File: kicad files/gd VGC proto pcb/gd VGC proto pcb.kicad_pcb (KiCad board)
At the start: 2 copper layers, 104 parts, among them J1 PWR_IN, J10 VID_OUT, J11 RCA MONO OUT, J12 Main Data Bus, J13 Mono-Color, J14 Mono-Color, J15 VBL, J16 RTC, J17 RCA Shunt Select, J18 RCA, J19 CREF, J2 Video Binary B, J20 RGB In, J21 CLKS, J22 Memory Control, J23 VGC Extra, J3 Aux Data Bus, J4 DAC RGB, J5 Video Binary G, J6 COMP_RGB, J7 Video Binary R, J8 RAM Addr Bus, J9 Composite Sync, Q1 BC817, Q2 BC817, Q3 BC817, U1 MIC5504-3.3YM5, U2 28.636360 MHz

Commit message: most of VGC routed
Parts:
- removed TP160, TP189, TP5: TestPoint, My Libraries:Harwin-S1751-46-Test-Point
- added C16: 1000u, Capacitor_THT:CP_Radial_D5.0mm_P2.50mm, F.Cu at (106.7, 75.2)
- added J24: CLK_PH0, Connector_PinHeader_2.54mm:PinHeader_1x02_P2.54mm_Vertical, F.Cu at (129.5, 130.8)
- added J25: Bald-Ext-1, Connector_PinHeader_2.54mm:PinHeader_2x20_P2.54mm_Vertical, F.Cu at (86.4, 80.0)
- added J26: SYNC, Connector_PinHeader_2.54mm:PinHeader_1x02_P2.54mm_Vertical, F.Cu at (121.9, 130.8)
- C59, R11, R196, TP112, TP93: moved to B.Cu
- C61: footprint Capacitor_SMD:C_0805_2012Metric -> Capacitor_THT:CP_Radial_D5.0mm_P2.50mm
- J13: value Mono-Color -> COMSYNC
- J19: footprint Connector_PinHeader_2.54mm:PinHeader_1x02_P2.54mm_Vertical -> Connector_PinHeader_2.54mm:PinHeader_2x02_P2.54mm_Vertical
- J20: footprint Connector_PinHeader_2.54mm:PinHeader_1x04_P2.54mm_Vertical -> Connector_PinHeader_2.54mm:PinHeader_1x08_P2.54mm_Vertical
- J21: value CLKS -> CLK_14M; footprint Connector_PinHeader_2.54mm:PinHeader_1x04_P2.54mm_Vertical -> Connector_PinHeader_2.54mm:PinHeader_1x02_P2.54mm_Vertical
- J22: footprint Connector_PinHeader_2.54mm:PinHeader_1x06_P2.54mm_Vertical -> Connector_PinHeader_2.54mm:PinHeader_2x06_P2.54mm_Vertical
- J23: footprint Connector_PinHeader_2.54mm:PinHeader_1x03_P2.54mm_Vertical -> Connector_PinHeader_2.54mm:PinHeader_2x03_P2.54mm_Vertical
- moved R206 145.1 mm to (100.3, 76.2), turned to 270 degrees
- moved J5 114.3 mm to (120.7, 72.4)
- moved J7 109.5 mm to (130.8, 80.0), turned to 180 degrees
- moved C61 107.1 mm to (130.8, 86.9), turned to 90 degrees
- moved J2 104.4 mm to (141.0, 80.0), turned to 180 degrees
- moved C30 99.4 mm to (127.3, 125.2)
- moved C59 83.3 mm to (137.2, 110.2), turned to 90 degrees
- moved J15 79.0 mm to (143.5, 102.9)
- moved TP112 67.8 mm to (137.2, 114.3), turned to 180 degrees
- moved R30 65.3 mm to (127.3, 127.5), turned to 180 degrees
- moved R196 60.1 mm to (123.7, 126.0), turned to 270 degrees
- moved TP93 57.8 mm to (127.5, 125.7), turned to 90 degrees
- moved R11 52.9 mm to (131.1, 126.0), turned to 270 degrees
- moved J20 29.2 mm to (96.5, 88.9), turned to 0 degrees
- moved J8 20.5 mm to (96.5, 110.5), turned to 0 degrees
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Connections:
- J19 pad 2: CREF.L -> CREF.H
- J20 pad 1: /RGB1.H -> /RGB4.H
- J20 pad 2: /RGB2.H -> /RGB4.H
- J20 pad 3: /RGB4.H -> /RGB8.H
- J21 pad 1: /14M.H -> /14MD.H
- J22 pad 1: /A2R-W.H -> /FLIP6.H
- J22 pad 2: /STRETCH.L -> /FLIP6.H
- J22 pad 4: /FLIP6.H -> /FLIP7.H
- J22 pad 5: /IRQ.L -> /HDSEL.H
- J22 pad 6: /M2SEL.L -> /HDSEL.H
- J23 pad 1: /RESET.L -> /IRQ.L
- J23 pad 2: /HDSEL.H -> /IRQ.L
- J23 pad 3: /BABUS12 -> /RESET.L
- UF2 pad 55: /UG3-6 -> /UG3-1
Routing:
- net /PH0.H: track 0.00 -> 61.5 mm
- net /RABUS6: track 0.00 -> 47.2 mm
- net /RABUS7: track 0.00 -> 46.6 mm
- net /RABUS4: track 0.00 -> 42.7 mm
- net /RABUS2: track 0.00 -> 42.6 mm
- net /RABUS5: track 0.00 -> 41.6 mm
- net /RABUS1: track 0.00 -> 41.0 mm
- net /RABUS3: track 0.00 -> 39.9 mm
- net /RABUS0: track 0.00 -> 38.5 mm
- net /MDBUS6: track 0.00 -> 34.5 mm
- net /MDBUS7: track 0.00 -> 34.1 mm
- net /ADBUS7: track 0.00 -> 30.6 mm
- net /MDBUS4: track 0.00 -> 30.3 mm
- net /ADBUS0: track 0.00 -> 30.1 mm
- net /MDBUS1: track 0.00 -> 30.1 mm
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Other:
- copper layers 2 -> 4
- net class Default: trace_width 0.2032 -> 0.254

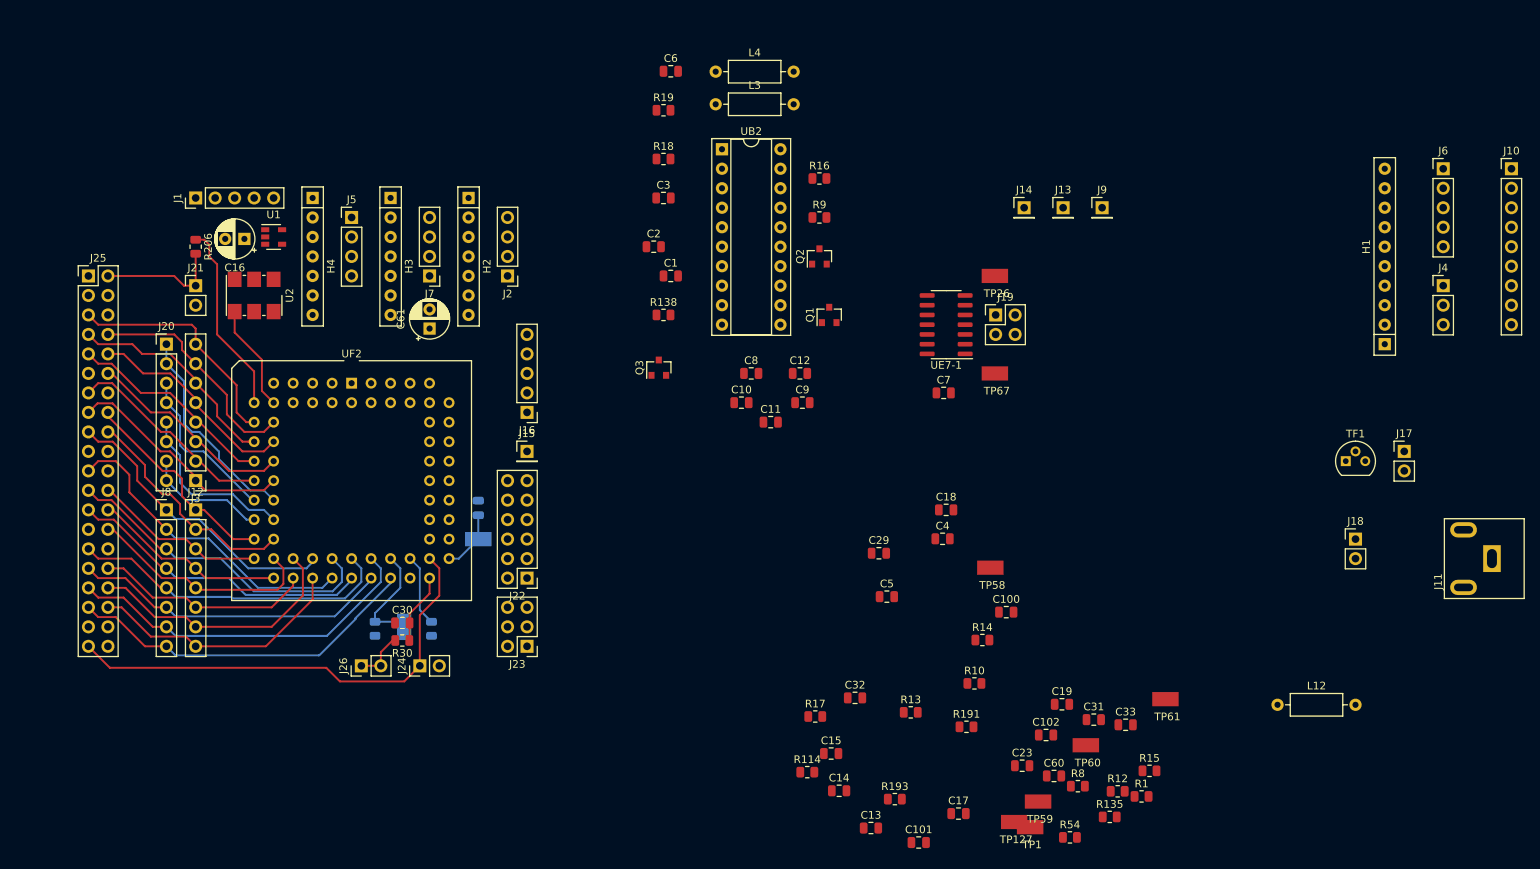
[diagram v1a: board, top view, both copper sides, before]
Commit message: More grouping components by function. Fixed an error with filtering caps on RGB near video output connector.
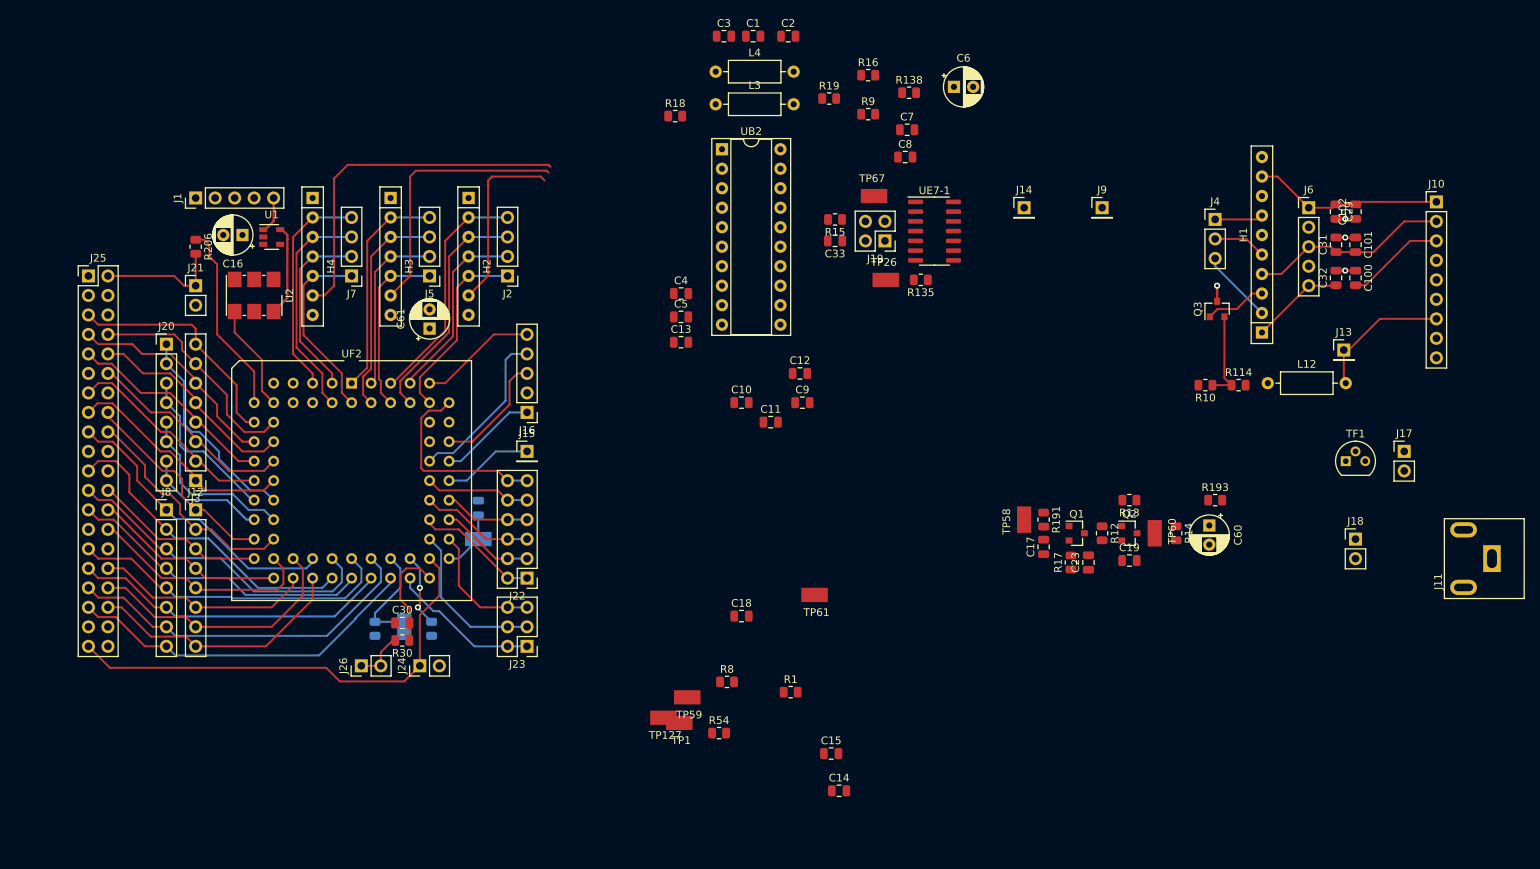
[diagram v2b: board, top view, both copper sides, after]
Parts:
- C6, C60: footprint Capacitor_SMD:C_0805_2012Metric -> Capacitor_THT:CP_Radial_D5.0mm_P2.50mm
- moved C101 96.5 mm to (251.5, 75.9), turned to 270 degrees
- moved C32 83.2 mm to (248.9, 80.3), turned to 90 degrees
- moved R15 82.7 mm to (183.6, 72.6), turned to 180 degrees
- moved C102 79.2 mm to (251.5, 71.6), turned to 90 degrees
- moved R114 75.5 mm to (236.2, 94.2)
- moved C29 74.4 mm to (248.9, 71.6), turned to 270 degrees
- moved R135 74.2 mm to (194.8, 80.5), turned to 180 degrees
- moved C33 73.5 mm to (183.6, 75.4), turned to 180 degrees
- moved Q3 73.1 mm to (233.4, 84.3)
- moved C31 69.5 mm to (248.9, 75.9), turned to 90 degrees
- moved C13 68.0 mm to (163.6, 88.6)
- moved C100 63.0 mm to (251.5, 80.3), turned to 270 degrees
- moved R193 57.1 mm to (233.2, 109.2)
- moved Q2 54.1 mm to (222.0, 113.5), turned to 0 degrees
- moved R10 49.2 mm to (231.9, 94.2), turned to 180 degrees
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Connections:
- C16 pad 1: Net-(C16-Pad1) -> +5V
- C61 pad 1: Net-(C16-Pad1) -> +5V
- J10 pad 1: /COMSYNC -> /COMP-BLUE
- J10 pad 2: /COMP-RED -> /COMP-GREEN
- J10 pad 3: /COMP-GREEN -> /COMP-RED
- J10 pad 4: /COMP-BLUE -> Net-(J10-Pad4)
- J10 pad 6: GND -> Net-(J10-Pad6)
- J10 pad 7: Net-(J10-Pad7) -> /COMSYNC
- UF2 pad 55: /UG3-1 -> /UG3-6
- UF2 pad 58: Net-(C16-Pad1) -> +5V
- UF2 pad 8: Net-(C16-Pad1) -> +5V
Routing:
- net /H4-6: track 0.00 -> 46.3 mm
- net /H3-6: track 0.00 -> 35.0 mm
- net /VID3: track 0.00 -> 31.0 mm
- net /VID2: track 0.00 -> 30.9 mm
- net /VID10: track 0.00 -> 29.5 mm
- net /VID11: track 0.00 -> 28.8 mm
- net /VID7: track 0.00 -> 28.8 mm
- net /VID6: track 0.00 -> 28.6 mm
- net /COMP-GREEN: track 0.00 -> 26.2 mm
- net /STRETCH.L: track 0.00 -> 25.5 mm
- net /COMP-RED: track 0.00 -> 25.1 mm
- net /VID1: track 0.00 -> 24.7 mm
- net /VID0: track 0.00 -> 24.7 mm
- net /COMP-BLUE: track 0.00 -> 24.7 mm
- net /VID8: track 0.00 -> 24.7 mm
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- added copper zone on In2.Cu, net +5V
- added copper zone on In1.Cu, net GND

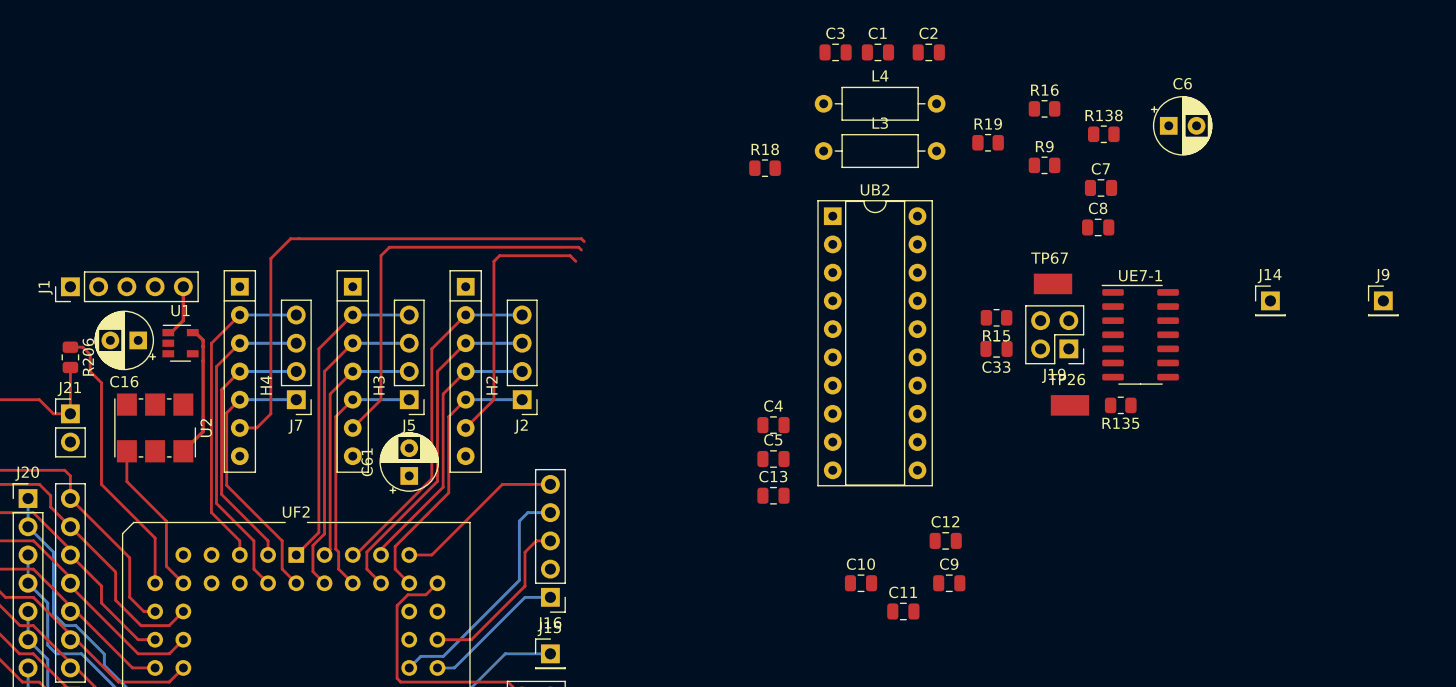
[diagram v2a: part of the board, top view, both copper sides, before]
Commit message: changed some caps to electrolytics and fixed existing diameters to be realistic. better placements around the 1377
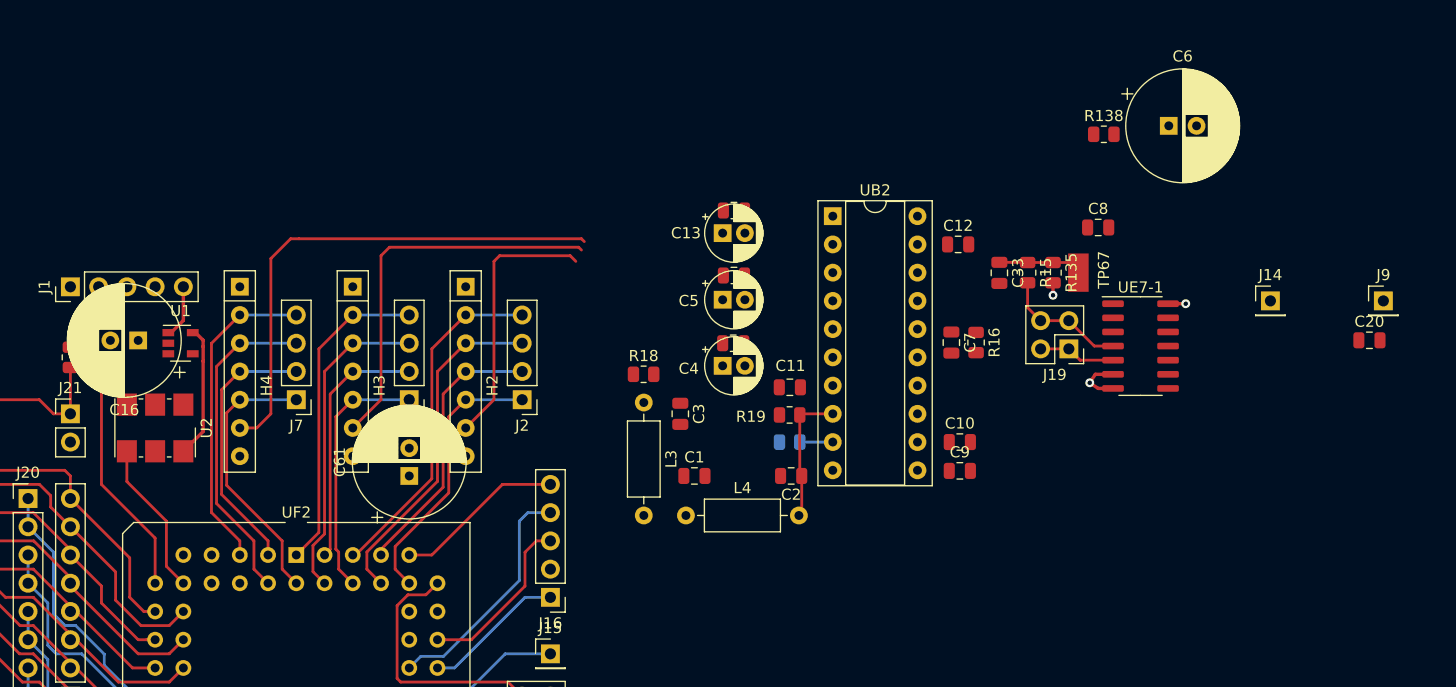
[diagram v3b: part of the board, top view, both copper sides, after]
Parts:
- removed TP26: TestPoint, My Libraries:Harwin-S1751-46-Test-Point
- added C20: 100n, Capacitor_SMD:C_0805_2012Metric, F.Cu at (217.2, 74.7)
- added C4alt1: 22uF, Capacitor_SMD:C_0805_2012Metric, F.Cu at (160.0, 74.9)
- added C5alt1: 22uF, Capacitor_SMD:C_0805_2012Metric, F.Cu at (160.0, 68.8)
- added C6alt1: 22uF, Capacitor_SMD:C_0805_2012Metric, F.Cu at (160.0, 63.0)
- C13, C4, C5: footprint Capacitor_SMD:C_0805_2012Metric -> Capacitor_THT:CP_Radial_D5.0mm_P2.00mm
- C16, C6, C61: footprint Capacitor_THT:CP_Radial_D5.0mm_P2.50mm -> Capacitor_THT:CP_Radial_D10.0mm_P2.50mm
- R9: moved to B.Cu
- moved C1 41.5 mm to (156.5, 86.9)
- moved C2 40.1 mm to (165.2, 86.9), turned to 180 degrees
- moved L4 39.1 mm to (155.7, 90.4)
- moved C3 35.4 mm to (155.2, 81.3), turned to 270 degrees
- moved R9 33.8 mm to (165.0, 83.8)
- moved R19 30.3 mm to (165.0, 81.4)
- moved L3 27.8 mm to (151.9, 80.3), turned to 270 degrees
- moved C12 26.7 mm to (180.2, 66.0)
- moved C13 24.1 mm to (159.0, 65.0)
- moved C11 22.6 mm to (165.0, 78.9), turned to 180 degrees
- moved R16 21.9 mm to (181.8, 74.9), turned to 270 degrees
- moved R18 21.5 mm to (151.9, 77.7)
- moved C7 19.4 mm to (179.6, 74.9), turned to 270 degrees
- moved C10 15.5 mm to (180.3, 83.8)
- moved C5 15.0 mm to (159.0, 71.0)
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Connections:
- C13 pad 1: /UC2-3 -> /H4-6
- C13 pad 2: /H4-6 -> /UC2-3
- C4 pad 1: /UC2-5 -> /H2-6
- C4 pad 2: /H2-6 -> /UC2-5
- C5 pad 1: /UC2-4 -> /H3-6
- C5 pad 2: /H3-6 -> /UC2-4
- UE7-1 pad 14: (no net) -> +5V
- UE7-1 pad 7: (no net) -> GND
- UF2 pad 55: /UG3-6 -> /UG3-1
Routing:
- net /UC2-8: track 0.00 -> 12.2 mm
- net CREF.L: track 0.00 -> 11.4 mm
- net /R135-1: track 0.00 -> 8.58 mm
- net CREF.H: track 0.00 -> 6.94 mm
- net GND: track 7.62 -> 14.0 mm, vias 3 -> 5
- net /UC2-9: track 0.00 -> 2.97 mm
- net +5V: track 4.59 -> 6.17 mm, vias 0 -> 1

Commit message: 0 Unrouted!!
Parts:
- removed TP58: TestPoint, My Libraries:Harwin-S1751-46-Test-Point
- added C21: 10u, Capacitor_THT:CP_Radial_D5.0mm_P2.50mm, F.Cu at (105.4, 73.7)
- added C22: 10u, Capacitor_THT:CP_Radial_D5.0mm_P2.50mm, F.Cu at (120.4, 86.4)
- added C24: 10u, Capacitor_THT:CP_Radial_D5.0mm_P2.50mm, F.Cu at (183.4, 71.4)
- added C25: 1u, Capacitor_SMD:C_0805_2012Metric, F.Cu at (180.5, 99.4)
- added J27: 12V_IN, Connector_PinHeader_2.54mm:PinHeader_1x02_P2.54mm_Vertical, F.Cu at (179.2, 71.1)
- added J28: -5V_In, Connector_PinHeader_2.54mm:PinHeader_1x02_P2.54mm_Vertical, F.Cu at (147.4, 67.9)
- added TP2: TestPoint, My Libraries:Harwin-S1751-46-Test-Point, F.Cu at (172.0, 127.0)
- added TP3: TestPoint, My Libraries:Harwin-S1751-46-Test-Point, F.Cu at (187.5, 82.9)
- added TP4: TestPoint, My Libraries:Harwin-S1751-46-Test-Point, F.Cu at (149.9, 93.7)
- added TP5: TestPoint, My Libraries:Harwin-S1751-46-Test-Point, F.Cu at (94.5, 83.2)
- C16, C61: value 1000u -> 470u
- J1: value PWR_IN -> +5V_IN; footprint Connector_PinHeader_2.54mm:PinHeader_1x05_P2.54mm_Vertical -> Connector_PinHeader_2.54mm:PinHeader_1x03_P2.54mm_Vertical
- moved H1 121.0 mm to (120.3, 65.3), turned to 0 degrees
- moved J4 118.3 mm to (115.1, 65.5), turned to 270 degrees
- moved C14 111.4 mm to (100.8, 73.2)
- moved C102 97.5 mm to (153.9, 71.0), turned to 180 degrees
- moved C15 97.2 mm to (110.2, 78.0), turned to 180 degrees
- moved C29 95.0 mm to (153.9, 68.6), turned to 0 degrees
- moved J10 93.5 mm to (168.7, 65.4), turned to 90 degrees
- moved C101 93.1 mm to (158.5, 70.9), turned to 180 degrees
- moved J6 92.5 mm to (153.0, 65.4), turned to 90 degrees
- moved C31 90.7 mm to (158.5, 68.6), turned to 0 degrees
- moved C100 89.0 mm to (162.9, 70.7), turned to 180 degrees
- moved C32 86.8 mm to (162.9, 68.6), turned to 0 degrees
- moved J11 86.7 mm to (182.9, 125.0), turned to 0 degrees
- moved J14 81.8 mm to (148.8, 127.3), turned to 270 degrees
- moved Q3 75.0 mm to (159.0, 75.1), turned to 180 degrees
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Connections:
- J1 pad 2: Net-(J1-Pad2) -> GND
- J1 pad 3: +12V -> +5V
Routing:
- net /COMP-SYN: track 8.05 -> 107.7 mm, vias 0 -> 1
- net +12V: track 2.05 -> 92.4 mm, vias 1 -> 2
- net /MONO-COLOR: track 0.00 -> 86.1 mm, vias 0 -> 1
- net /R54-2: track 0.00 -> 60.3 mm
- net /COMP-RED: track 25.1 -> 64.5 mm
- net GND: track 14.0 -> 52.6 mm, vias 5 -> 31
- net /UC2-13: track 0.00 -> 37.7 mm
- net /UC2-10: track 0.00 -> 31.9 mm
- net /H3-6: track 35.0 -> 63.2 mm
- net /COMP-GREEN: track 26.2 -> 53.7 mm
- net /H4-6: track 46.3 -> 71.1 mm
- net /UC2-16: track 0.37 -> 22.2 mm
- net /H2-1: track 6.31 -> 28.0 mm, vias 0 -> 1
- net /UC2-9: track 2.97 -> 22.7 mm, vias 0 -> 1
- net /J11-1: track 0.00 -> 19.6 mm
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- added copper zone on B.Cu, net GND
- added copper zone on F.Cu, net GND
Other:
- board outline added: 114.3 x 73.7 mm
